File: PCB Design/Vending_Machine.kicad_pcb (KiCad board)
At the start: 2 copper layers, 116.6 x 143.7 mm, 177 parts, among them J1 Mains, J11 Conn_Aux, J12 Conn_Sig, J13 Conn_I2C, J14 Conn_I2C, J2 Conn_IO, J3 Conn_IO11, J31 GPIO3, J32 GPIO2, J33 SPI, J34 Conn_01x15, J35 UART0, J36 Display, J37 Conn_01x15, J38 GPIO1, J39 I2C, J4 Conn_IO12, J42 Conn, J43 Conn_I2C, J44 I2C, J46 Conn_I2C, J47 Conn_Sig, SW31 EN, SW32 BOOT, U11 AMS1117-3.3, U12 SX1509BIULTRT, U13 TCA9406DC, U31 AMS1117-3.3, U32 TCA9406DC, U33 ESP32-WROOM-32UE, U41 AMS1117-3.3, U42 SX1509BIULTRT, U43 TCA9406DC

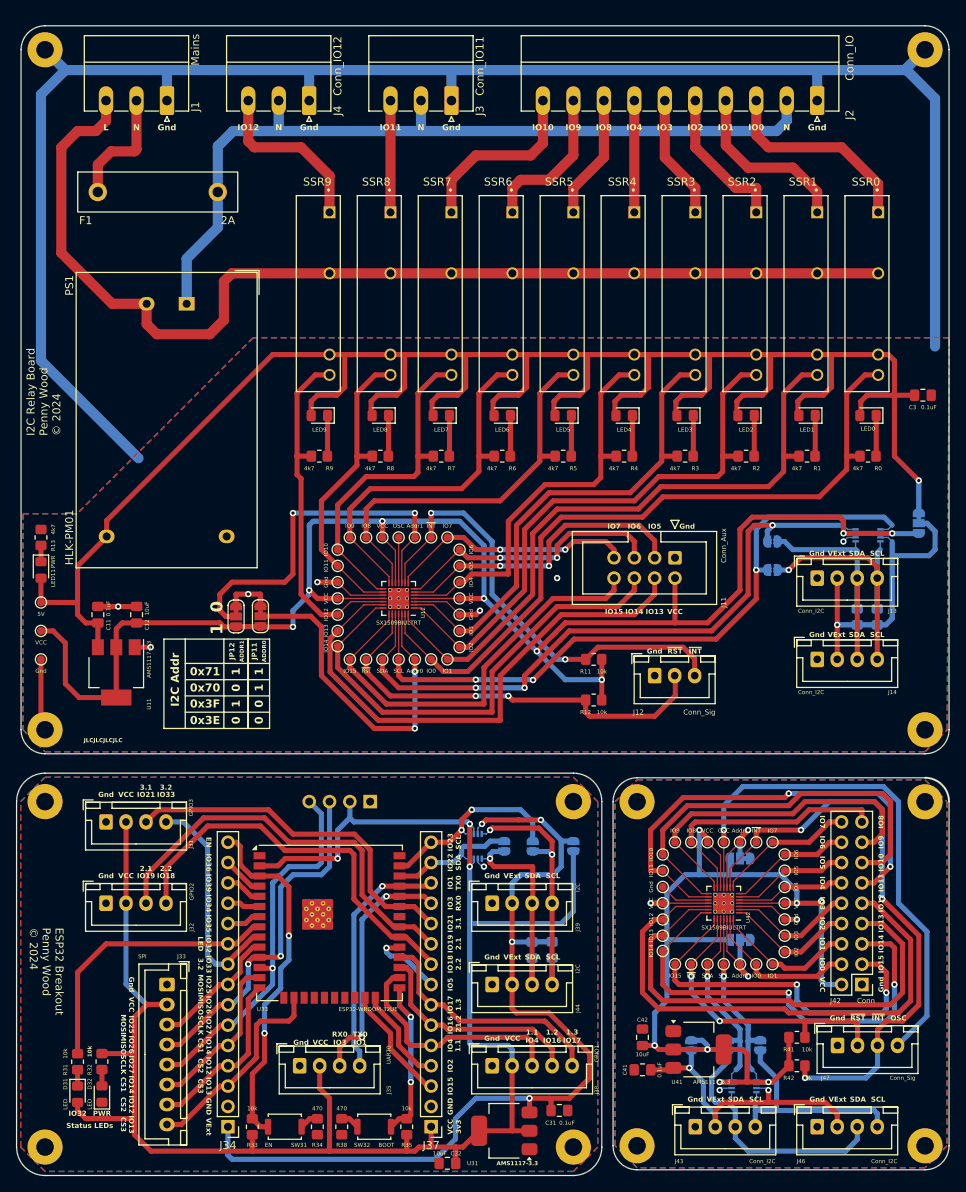
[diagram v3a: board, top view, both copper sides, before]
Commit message: Add OSCIO pin and voltage section silk-screen
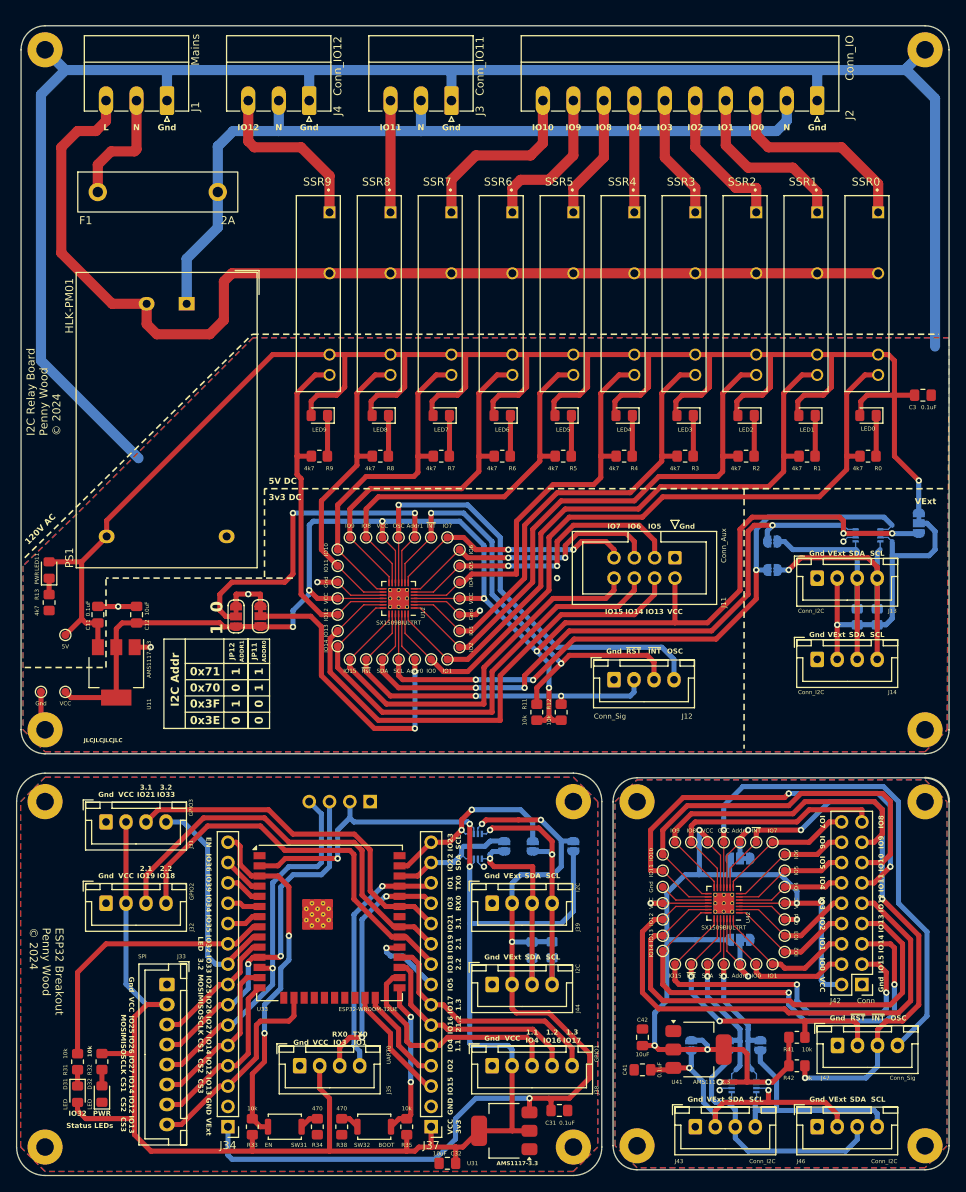
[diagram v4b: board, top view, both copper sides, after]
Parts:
- J12: footprint Connector_JST:JST_XH_B3B-XH-A_1x03_P2.50mm_Vertical -> Connector_JST:JST_XH_B4B-XH-A_1x04_P2.50mm_Vertical
- moved R11 9.71 mm to (112.3, 133.6), turned to 90 degrees
- moved VCC 8.21 mm to (53.3, 131.1)
- moved R13 8.20 mm to (51.3, 119.9), turned to -90 degrees
- moved J12 5.11 mm to (121.9, 129.5)
- moved 5V 5.08 mm to (53.3, 124.0)
- moved R12 4.34 mm to (115.3, 133.6), turned to 90 degrees
- moved Gnd 4.06 mm to (50.3, 131.1)
- moved LED11 1.02 mm to (51.3, 115.8), turned to 90 degrees
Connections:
- OSC pad 11: unconnected-(U12-OSCIO-Pad11) -> /Relay Controller/OSCIO
- U12 pad 11: unconnected-(U12-OSCIO-Pad11) -> /Relay Controller/OSCIO
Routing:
- net /Relay Controller/OSCIO: track 0.00 -> 58.6 mm, vias 0 -> 1
- net /Relay Controller/VCC: track 210.9 -> 199.2 mm
- net /Relay Controller/~{RST}: track 53.5 -> 46.1 mm
- net unconnected-(U12-OSCIO-Pad11): track 5.68 -> 0.00 mm
- net /Relay Controller/GND: track 258.3 -> 254.3 mm
- net /Relay Controller/~{INT}: track 57.8 -> 58.9 mm
- net /Relay Controller/+5V: track 260.3 -> 259.2 mm
- net /Relay Controller/IO2: track 70.9 -> 70.3 mm
- net /Relay Controller/IO1: track 80.7 -> 80.1 mm
- net /Relay Controller/IO3: track 61.0 -> 60.4 mm
- net /Relay Controller/IO0: track 90.8 -> 90.2 mm
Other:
- board text added: "120V AC"
- board text added: "3v3 DC"
- board text added: "5V DC"

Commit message: Testpoints to schematic.
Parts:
- removed 5V, Addr0 (x2), Addr1 (x2), Gnd (x5), IO0 (x2), IO1 (x2), IO10 (x2), IO11 (x2), IO12 (x2), IO13 (x2), IO14 (x2), IO15 (x2), IO2, IO3 (x2), IO4 (x2), IO5, IO6 (x2), IO7 (x2), IO8 (x2), IO9 (x2), OSC (x2), SDA (x2), ~{INT} (x2), ~{Rst} (x2): , Footprints:TestPoint_Pad_D1.0mm
- removed C3: 0.1uF, Capacitor_SMD:C_0805_2012Metric_Pad1.18x1.45mm_HandSolder
- removed SCL (x2): SCL_VCC, Footprints:TestPoint_Pad_D1.0mm
- removed VCC (x2): 4, Footprints:TestPoint_Pad_D1.0mm
- removed VCC (x2): 18, Footprints:TestPoint_Pad_D1.0mm
- removed VCC (x2): 12, Footprints:TestPoint_Pad_D1.0mm
- removed VCC: VCC, Footprints:TestPoint_Pad_D1.0mm
- added C13: 0.1uF, Capacitor_SMD:C_0805_2012Metric_Pad1.18x1.45mm_HandSolder, F.Cu at (160.5, 94.0)
- added TP12: IO3, Footprints:TestPoint_Pad_D1.0mm, F.Cu at (102.6, 123.4)
- added TP13: VCC, Footprints:TestPoint_Pad_D1.0mm, F.Cu at (102.6, 119.4)
- added TP14: GND, Footprints:TestPoint_Pad_D1.0mm, F.Cu at (102.6, 121.4)
- added TP15: IO4, Footprints:TestPoint_Pad_D1.0mm, F.Cu at (102.6, 117.3)
- added TP17: IO6, Footprints:TestPoint_Pad_D1.0mm, F.Cu at (102.6, 113.3)
- added TP18: IO7, Footprints:TestPoint_Pad_D1.0mm, F.Cu at (101.1, 111.8)
- added TP19: ~{INT}, Footprints:TestPoint_Pad_D1.0mm, F.Cu at (99.1, 111.8)
- added TP20: ~{RST}, Footprints:TestPoint_Pad_D1.0mm, F.Cu at (90.9, 127.0)
- added TP21: VCC, Footprints:TestPoint_Pad_D1.0mm, F.Cu at (93.0, 111.8)
- added TP22: GND, Footprints:TestPoint_Pad_D1.0mm, F.Cu at (87.4, 117.3)
- added TP23: Addr0, Footprints:TestPoint_Pad_D1.0mm, F.Cu at (97.0, 127.0)
- added TP24: Addr1, Footprints:TestPoint_Pad_D1.0mm, F.Cu at (97.0, 111.8)
- added TP25: OSC, Footprints:TestPoint_Pad_D1.0mm, F.Cu at (95.0, 111.8)
- added TP26: SDA, Footprints:TestPoint_Pad_D1.0mm, F.Cu at (93.0, 127.0)
- added TP27: SCL, Footprints:TestPoint_Pad_D1.0mm, F.Cu at (95.0, 127.0)
- added TP28: VCC, Footprints:TestPoint_Pad_D1.0mm, F.Cu at (87.4, 119.4)
- added TP29: IO8, Footprints:TestPoint_Pad_D1.0mm, F.Cu at (90.9, 111.8)
- added TP30: IO9, Footprints:TestPoint_Pad_D1.0mm, F.Cu at (88.9, 111.8)
- added TP31: IO10, Footprints:TestPoint_Pad_D1.0mm, F.Cu at (87.4, 113.3)
- added TP32: IO11, Footprints:TestPoint_Pad_D1.0mm, F.Cu at (87.4, 115.3)
- added TP33: IO12, Footprints:TestPoint_Pad_D1.0mm, F.Cu at (87.4, 121.4)
- added TP34: IO13, Footprints:TestPoint_Pad_D1.0mm, F.Cu at (87.4, 123.4)
- added TP35: IO14, Footprints:TestPoint_Pad_D1.0mm, F.Cu at (87.4, 125.5)
- added TP36: IO15, Footprints:TestPoint_Pad_D1.0mm, F.Cu at (88.9, 127.0)
- added TP37: IO0, Footprints:TestPoint_Pad_D1.0mm, F.Cu at (99.1, 127.0)
- added TP38: IO1, Footprints:TestPoint_Pad_D1.0mm, F.Cu at (101.1, 127.0)
- added TP39: VCC, Footprints:TestPoint_Pad_D1.0mm, F.Cu at (133.6, 149.9)
- added TP40: ~{RST}, Footprints:TestPoint_Pad_D1.0mm, F.Cu at (131.6, 165.1)
- added TP41: ~{INT}, Footprints:TestPoint_Pad_D1.0mm, F.Cu at (139.7, 149.9)
- added TP42: Addr0, Footprints:TestPoint_Pad_D1.0mm, F.Cu at (137.7, 165.1)
- added TP43: Addr1, Footprints:TestPoint_Pad_D1.0mm, F.Cu at (137.7, 149.9)
- added TP44: OSC, Footprints:TestPoint_Pad_D1.0mm, F.Cu at (135.6, 149.9)
- added TP45: SDA, Footprints:TestPoint_Pad_D1.0mm, F.Cu at (133.6, 165.1)
- added TP46: SCL, Footprints:TestPoint_Pad_D1.0mm, F.Cu at (135.6, 165.1)
- added TP47: GND, Footprints:TestPoint_Pad_D1.0mm, F.Cu at (143.3, 159.5)
- added TP48: VCC, Footprints:TestPoint_Pad_D1.0mm, F.Cu at (143.3, 157.5)
- added TP49: IO0, Footprints:TestPoint_Pad_D1.0mm, F.Cu at (139.7, 165.1)
- added TP50: IO1, Footprints:TestPoint_Pad_D1.0mm, F.Cu at (141.7, 165.1)
- added TP51: IO2, Footprints:TestPoint_Pad_D1.0mm, F.Cu at (143.3, 163.6)
- added TP52: IO3, Footprints:TestPoint_Pad_D1.0mm, F.Cu at (143.3, 161.5)
- added TP53: IO4, Footprints:TestPoint_Pad_D1.0mm, F.Cu at (143.3, 155.4)
- added TP54: IO5, Footprints:TestPoint_Pad_D1.0mm, F.Cu at (143.3, 153.4)
- added TP55: IO6, Footprints:TestPoint_Pad_D1.0mm, F.Cu at (143.3, 151.4)
- added TP56: IO7, Footprints:TestPoint_Pad_D1.0mm, F.Cu at (141.7, 149.9)
- added TP57: GND, Footprints:TestPoint_Pad_D1.0mm, F.Cu at (128.0, 155.4)
- added TP58: VCC, Footprints:TestPoint_Pad_D1.0mm, F.Cu at (128.0, 157.5)
- added TP59: IO8, Footprints:TestPoint_Pad_D1.0mm, F.Cu at (131.6, 149.9)
- added TP60: IO9, Footprints:TestPoint_Pad_D1.0mm, F.Cu at (129.5, 149.9)
- added TP61: IO10, Footprints:TestPoint_Pad_D1.0mm, F.Cu at (128.0, 151.4)
- added TP62: IO11, Footprints:TestPoint_Pad_D1.0mm, F.Cu at (128.0, 153.4)
- added TP63: IO12, Footprints:TestPoint_Pad_D1.0mm, F.Cu at (128.0, 159.5)
- added TP64: IO13, Footprints:TestPoint_Pad_D1.0mm, F.Cu at (128.0, 161.5)
- added TP65: IO14, Footprints:TestPoint_Pad_D1.0mm, F.Cu at (128.0, 163.6)
- added TP66: IO15, Footprints:TestPoint_Pad_D1.0mm, F.Cu at (129.5, 165.1)
- added TP67: VCC, Footprints:TestPoint_Pad_D1.0mm, F.Cu at (53.3, 131.1)
- added TP68: GND, Footprints:TestPoint_Pad_D1.0mm, F.Cu at (50.3, 131.1)
- added TP69: 5V, Footprints:TestPoint_Pad_D1.0mm, F.Cu at (53.3, 124.0)
- TP11: renamed from IO2; value (none) -> IO2
- TP16: renamed from IO5; value (none) -> IO5
- turned D31 to 90 degrees
- renumbered H31 to H41, H31 to H42, H31 to H43, H31 to H44
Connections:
- D31 pad 1: Net-(D31-K) -> /Logic Controller/GND
- D31 pad 2: /Logic Controller/VCC -> Net-(D31-A)
- R31 pad 1: Net-(D31-K) -> Net-(D31-A)
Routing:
- net /Logic Controller/VCC: track 229.8 -> 221.2 mm
- net Net-(D31-K): track 2.04 -> 0.00 mm
- net Net-(D31-A): track 0.00 -> 2.04 mm
- net /Logic Controller/IO32: track 35.3 -> 34.1 mm

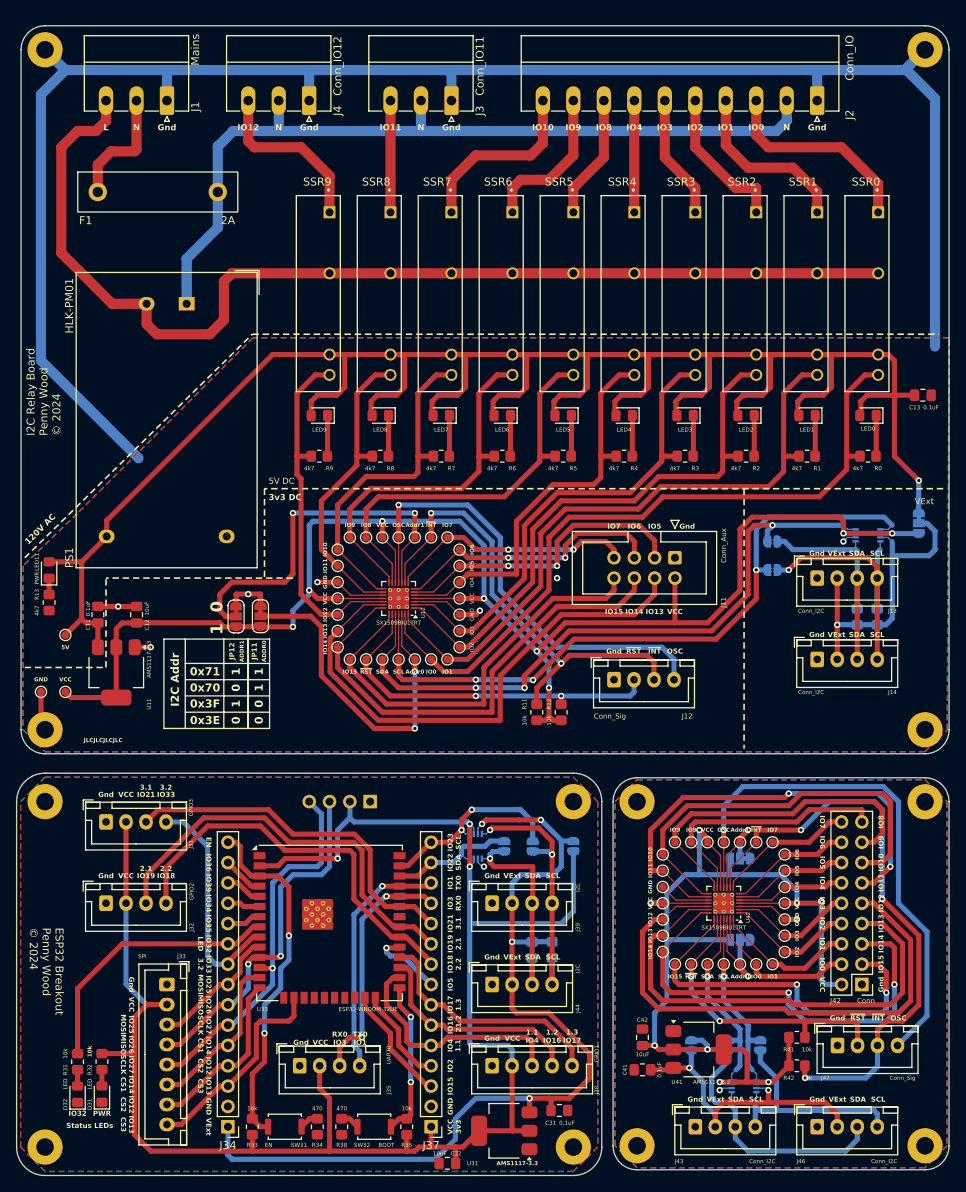
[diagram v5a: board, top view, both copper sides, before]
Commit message: Vcc->3v3 Added extra GPIO
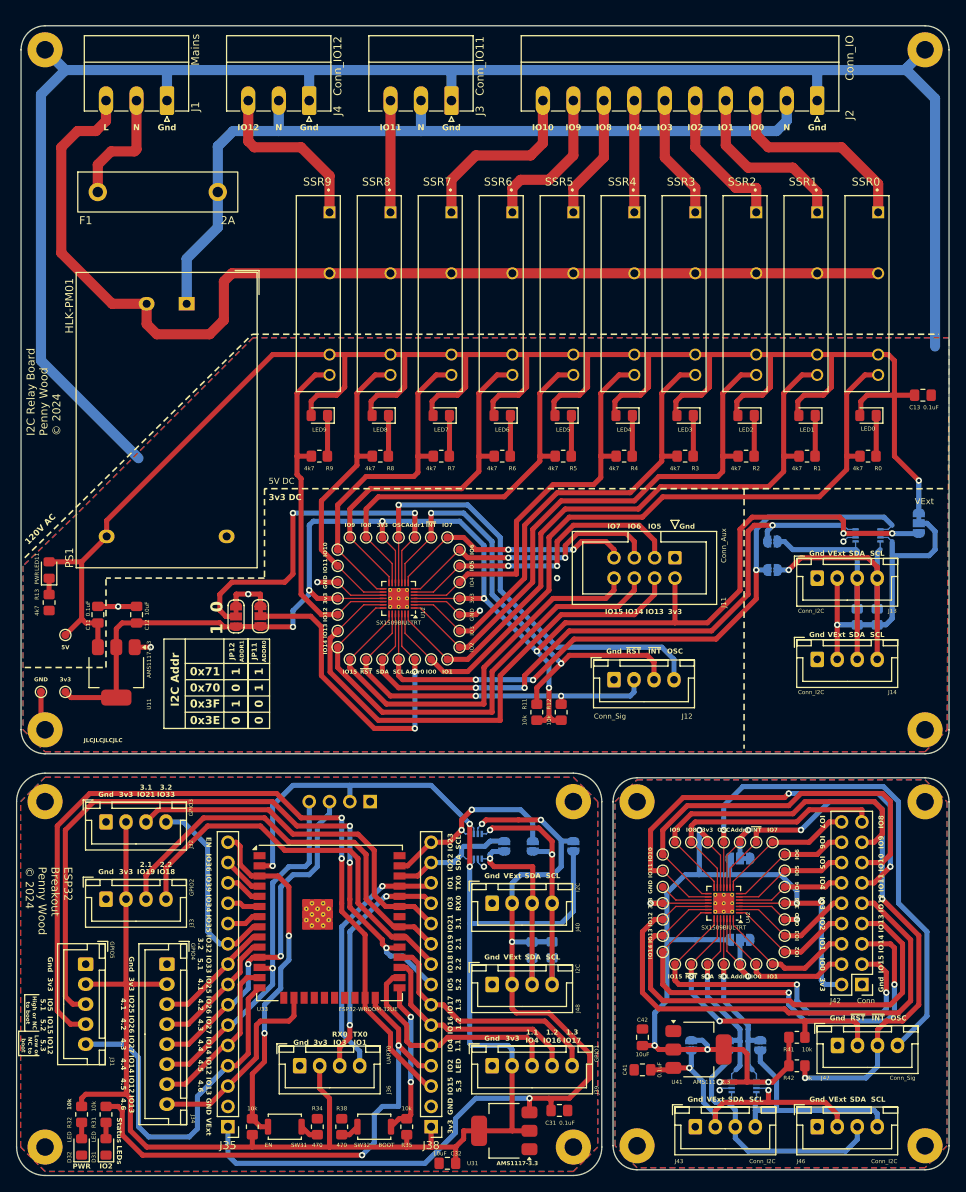
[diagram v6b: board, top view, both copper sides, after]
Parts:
- added J31: GPIO5, Connector_JST:JST_XH_B5B-XH-A_1x05_P2.50mm_Vertical, F.Cu at (55.9, 165.1)
- J34: renamed from J33; value SPI -> GPIO4
- JP14, JP42: value SCL_VCC -> SCL_3v3
- JP15, JP43: value SDA_VCC -> SDA_3v3
- JP33, JP41: value VCC_VExt -> VExt_3v3
- TP13, TP21, TP28, TP39, TP48, TP58, TP67: value VCC -> 3v3
- moved D31 7.49 mm to (58.4, 187.9)
- moved R31 7.49 mm to (58.4, 183.9)
- moved D32 7.08 mm to (55.4, 187.9)
- moved R32 7.08 mm to (55.4, 183.9)
- moved J34 2.54 mm to (66.0, 165.1)
- moved J33 0.51 mm to (58.4, 157.0)
- turned R34 to 90 degrees
- turned R38 to 90 degrees
- renumbered J31 to J32, J32 to J33, J34 to J35, J35 to J36, J36 to J37, J37 to J38, J38 to J39, J39 to J40, J44 to J48
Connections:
- net /IO Multiplexer/SCL_VCC renamed /IO Multiplexer/SCL_3v3
- net /IO Multiplexer/SDA_VCC renamed /IO Multiplexer/SDA_3v3
- net /IO Multiplexer/VCC renamed /IO Multiplexer/3v3
- net /Logic Controller/VCC renamed /Logic Controller/3v3
- net /Relay Controller/SCL_VCC renamed /Relay Controller/SCL_3v3
- net /Relay Controller/SDA_VCC renamed /Relay Controller/SDA_3v3
- net /Relay Controller/VCC renamed /Relay Controller/3v3
- J32 pad 4: /Logic Controller/IO33 -> /Logic Controller/IO32
- J34 pad 3: /Logic Controller/IO25 -> /Logic Controller/IO33
- J34 pad 4: /Logic Controller/IO26 -> /Logic Controller/IO25
- J34 pad 5: /Logic Controller/IO27 -> /Logic Controller/IO26
- J34 pad 6: /Logic Controller/IO14 -> /Logic Controller/IO27
- J34 pad 7: /Logic Controller/IO12 -> /Logic Controller/IO14
- R31 pad 2: /Logic Controller/IO32 -> /Logic Controller/IO2
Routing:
- net /Logic Controller/IO15: track 14.7 -> 104.3 mm, vias 0 -> 2
- net /Logic Controller/IO5: track 9.46 -> 88.6 mm, vias 1 -> 3
- net /Logic Controller/IO2: track 12.3 -> 65.4 mm, vias 0 -> 2
- net /Logic Controller/IO12: track 22.3 -> 46.4 mm
- net /Logic Controller/IO33: track 28.7 -> 15.2 mm
- net /Logic Controller/3v3: track 221.2 -> 232.6 mm
- net /Logic Controller/IO32: track 34.1 -> 25.1 mm
- net /Logic Controller/IO27: track 47.1 -> 45.0 mm
- net /Logic Controller/IO1: track 30.5 -> 31.8 mm
- net /Logic Controller/IO13: track 26.8 -> 25.7 mm
- net /Logic Controller/IO26: track 44.7 -> 43.7 mm
- net /Logic Controller/IO3: track 30.5 -> 29.6 mm
- net /Logic Controller/IO14: track 21.4 -> 20.7 mm
- net /Logic Controller/IO18: track 50.3 -> 49.8 mm
- net /Logic Controller/IO19: track 51.9 -> 51.4 mm
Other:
- board text added: "4.1"
- board text added: "4.2"
- board text added: "4.3"
- board text added: "4.4"
- board text added: "4.5"
- board text added: "4.6"
- board text added: "5.1"
- board text added: "5.2"
- board text added: "5.3"
- board text added: "High or NC to boot"
- board text added: "If VExt at 3v3: Switch JP13 Close JP14, JP15 Don't install U13"
- board text added: "If VExt powers 3v3: Also don't install U11"
- board text added: "Low or NC to boot"
- board text removed: "21.2"
- board text removed: "CS1"
- board text removed: "CS2"
- board text removed: "CS3"
- board text removed: "If VExt at VCC: Switch JP13 Close JP14, JP15 Don't install U13"
- board text removed: "If VExt powers VCC: Also don't install U11"
- board text removed: "MISO"
- board text removed: "MOSI"
- board text removed: "SCLK"
- board text removed: "VCC"
